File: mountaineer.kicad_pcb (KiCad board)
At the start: 2 copper layers, 79 x 50 mm, 71 parts, among them J1 USB_C_Receptacle, J2 CAT, J3 AUDIO, U1 TUSB2036, U2 FT232RL, U3 HS-100B, U4 TPS76333, U5 SN75240, U6 TPS2041, Y1 AWSCR-6.00CPLA

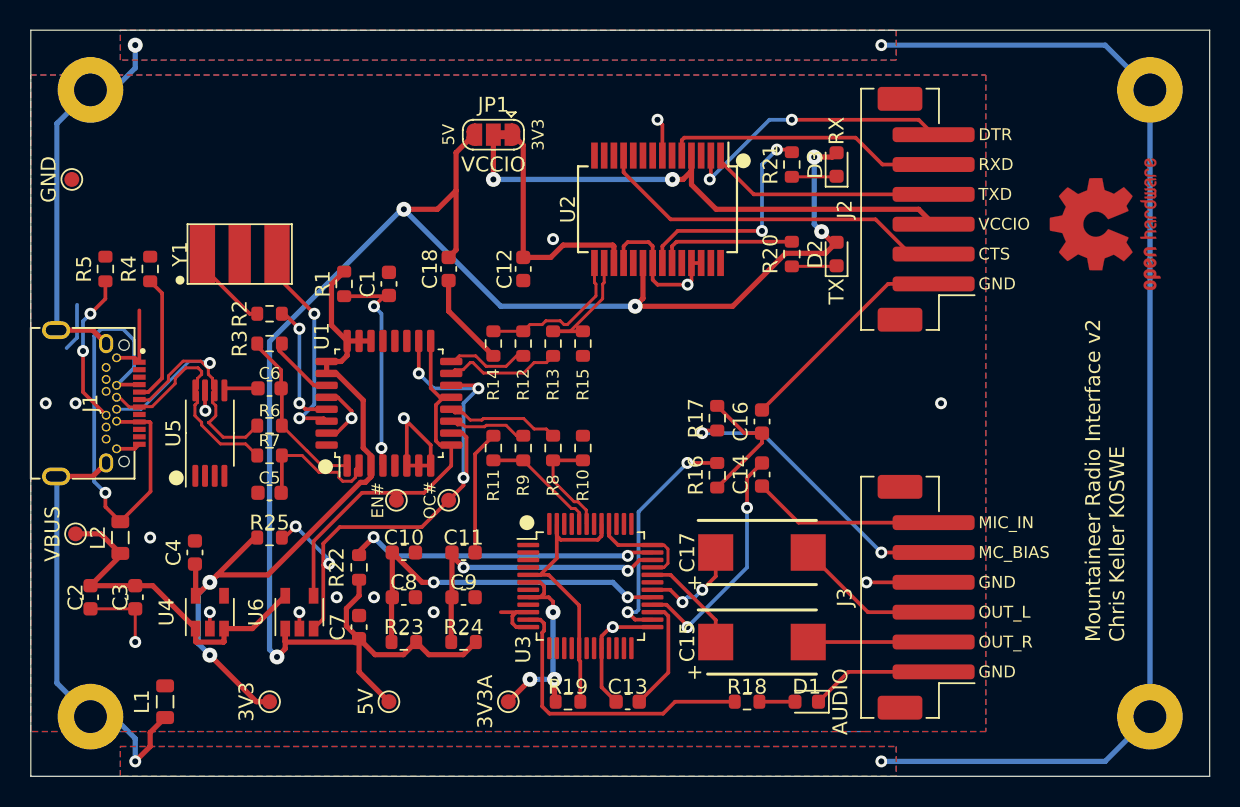
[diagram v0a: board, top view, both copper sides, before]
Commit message: Switch audio from HS100B to CM108B
The HS-100B is getting hard to find, but the CM108B is still available.
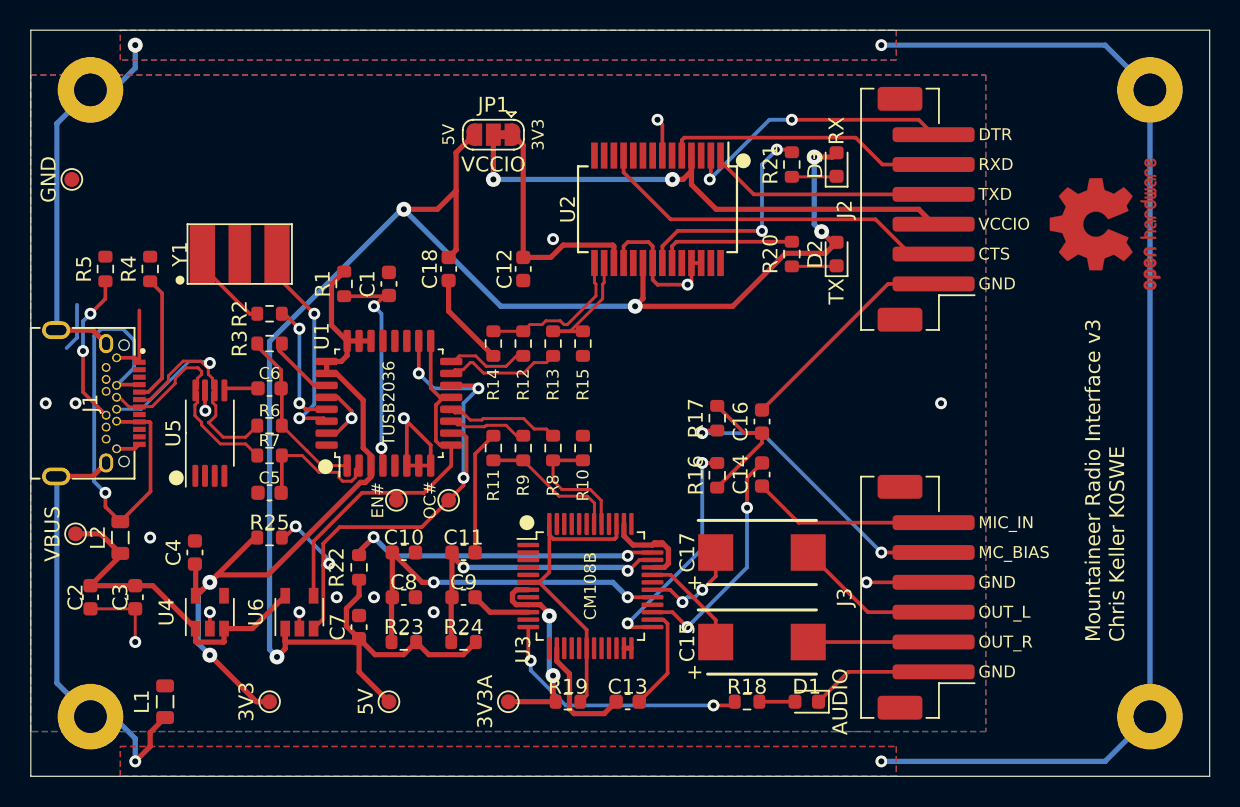
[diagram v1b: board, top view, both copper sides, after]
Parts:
- U3: value HS-100B -> CM108B
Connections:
- U3 pad 11: /LEDO -> (no net)
- U3 pad 12: GNDREF -> /LEDO
- U3 pad 14: (no net) -> GNDREF
- U3 pad 17: /HIDPU -> (no net)
- U3 pad 18: (no net) -> /HIDPU
- U3 pad 20: GNDREF -> (no net)
- U3 pad 23: (no net) -> GNDREF
- U3 pad 24: (no net) -> GNDREF
- U3 pad 25: GNDREF -> /VBIAS
- U3 pad 26: /VBIAS -> /VREF
- U3 pad 27: /VREF -> /MICIN
- U3 pad 28: /MICIN -> (no net)
- U3 pad 38: (no net) -> GNDREF
- U3 pad 39: (no net) -> /HIDPU
- U3 pad 40: GNDREF -> (no net)
- U3 pad 41: /HIDPU -> /U1+
- U3 pad 42: (no net) -> /U1-
- U3 pad 43: /U1+ -> (no net)
- U3 pad 44: /U1- -> (no net)
- U3 pad 47: /HIDPU -> (no net)
- U3 pad 48: (no net) -> /HIDPU
- U3 pad 5: /HIDPU -> (no net)
- U3 pad 6: /3V3A -> /HIDPU
- U3 pad 7: (no net) -> /3V3A
- U3 pad 8: /3V3A -> (no net)
- U3 pad 9: (no net) -> /3V3A
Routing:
- net /LEDO: track 20.2 -> 17.7 mm, vias 0 -> 2
- net /3V3A: track 15.3 -> 13.7 mm, vias 3 -> 2
- net GNDREF: track 110.3 -> 108.8 mm, vias 18 -> 17
- net /U1+: track 7.34 -> 8.73 mm
- net /U1-: track 7.99 -> 9.37 mm
- net /HIDPU: track 20.2 -> 21.4 mm
- net /VREF: track 7.72 -> 7.14 mm
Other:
- board text added: "Mountaineer Radio Interface v3 Chris Keller K0SWE"
- board text removed: "Mountaineer Radio Interface v2 Chris Keller K0SWE"
